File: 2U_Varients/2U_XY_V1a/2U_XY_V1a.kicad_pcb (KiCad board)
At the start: 4 copper layers, 83 x 212.6 mm, 32 parts, among them CN1 DF11-2DSA-4DP, J2 Conn_01x01, J3 Conn_01x01, J4 Conn_01x01, J5 Conn_01x01, U2 TMP112xxDRL, U3 DRV2605LDGS, U4 TCA4311ADGKR, U5 5040500691, U7 VEML6031X00

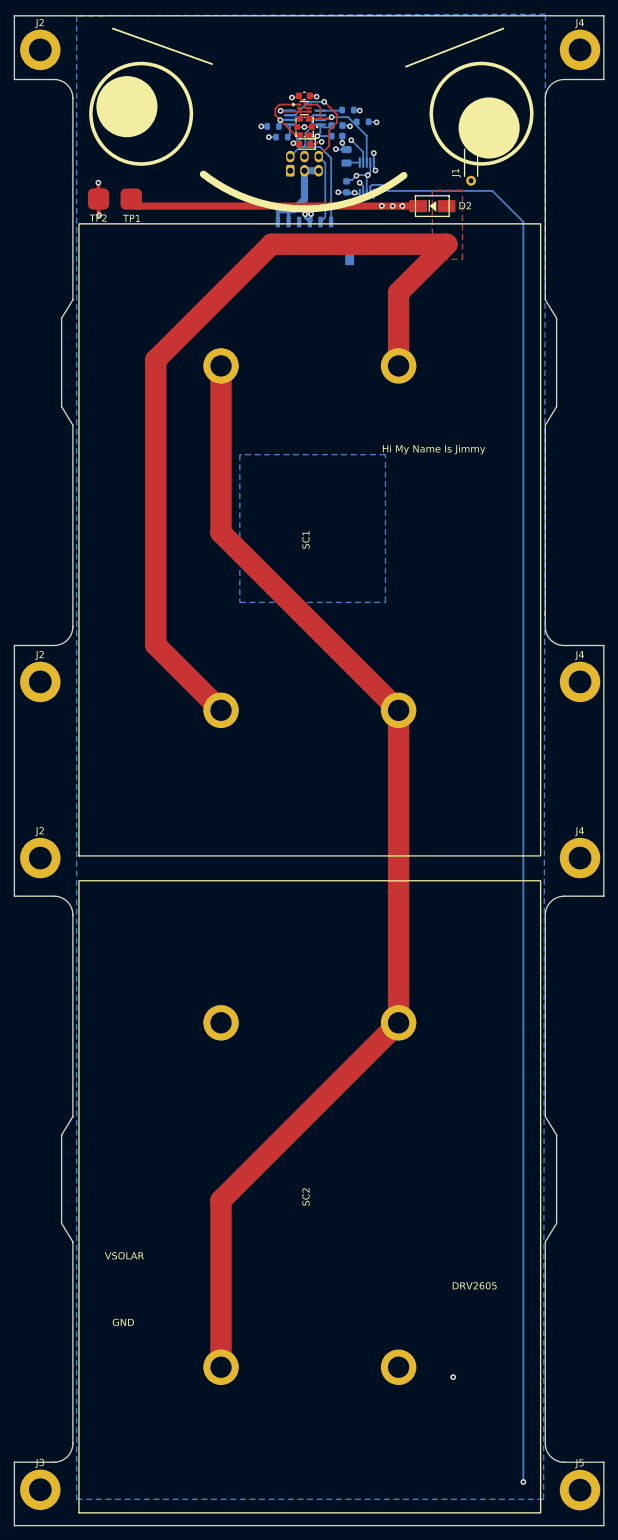
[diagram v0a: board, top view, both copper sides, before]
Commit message: Connector Adjustments
Moved away from the top of the Solar Face to the middle of the Solar Face
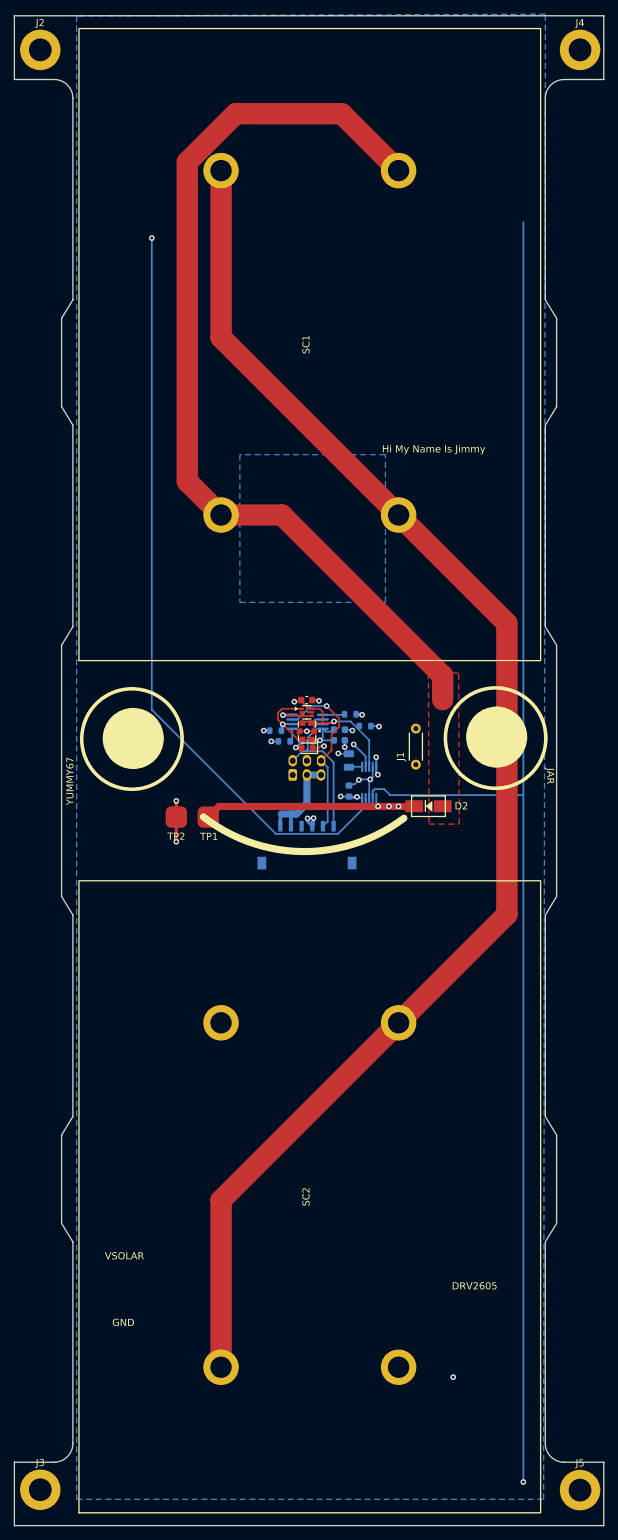
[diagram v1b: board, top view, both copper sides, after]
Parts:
- removed the J2 at (171.8, 154.8)
- removed the J2 at (171.8, 130.0)
- removed the J4 at (247.8, 154.8)
- removed the J4 at (247.8, 130.0)
- moved TP2 87.7 mm to (191.0, 149.0)
- moved TP1 87.7 mm to (195.5, 149.0)
- moved C2 85.1 mm to (209.3, 132.6)
- moved C3 85.1 mm to (215.3, 145.4)
- moved D4 85.1 mm to (209.4, 139.3)
- moved R2 85.1 mm to (206.2, 138.4)
- moved R4 85.1 mm to (215.5, 134.6)
- moved U3 85.1 mm to (218.1, 144.1)
- moved U4 85.1 mm to (209.4, 135.6)
- moved R6 85.1 mm to (217.5, 136.2)
- moved U2 85.1 mm to (209.3, 134.3)
- moved U5 85.1 mm to (209.3, 152.9)
- moved U7 85.1 mm to (209.3, 136.9)
- moved C4 85.1 mm to (213.9, 138.2)
- moved C5 85.1 mm to (215.3, 141.1)
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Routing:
- net Net-(U3-OUT+): track 20586.5 -> 20653.7 mm
- net Net-(SC1---Pad2): track 161.7 -> 201.8 mm
- net VSOLAR: track 55.9 -> 43.4 mm
- net /SOL_OUT: track 120.8 -> 131.5 mm
- net GND: track 26.8 -> 27.9 mm
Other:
- outline, holes or cut-outs redrawn
- board text added: "JAR"
- board text added: "V1a 2U Solar Panel Designed By: Michael Pham Reviewed By: William Hsu Modified By: Matthew Chang"
- board text added: "YUMMY67"
- board text removed: "V1a 2U Solar Panel Designed By: Michael Pham Reviewed By: William Hsu"

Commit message: Added GND and Clearance Holes
Moved clearance holes away and added 2 GND Vias for the Pico Molex Connector
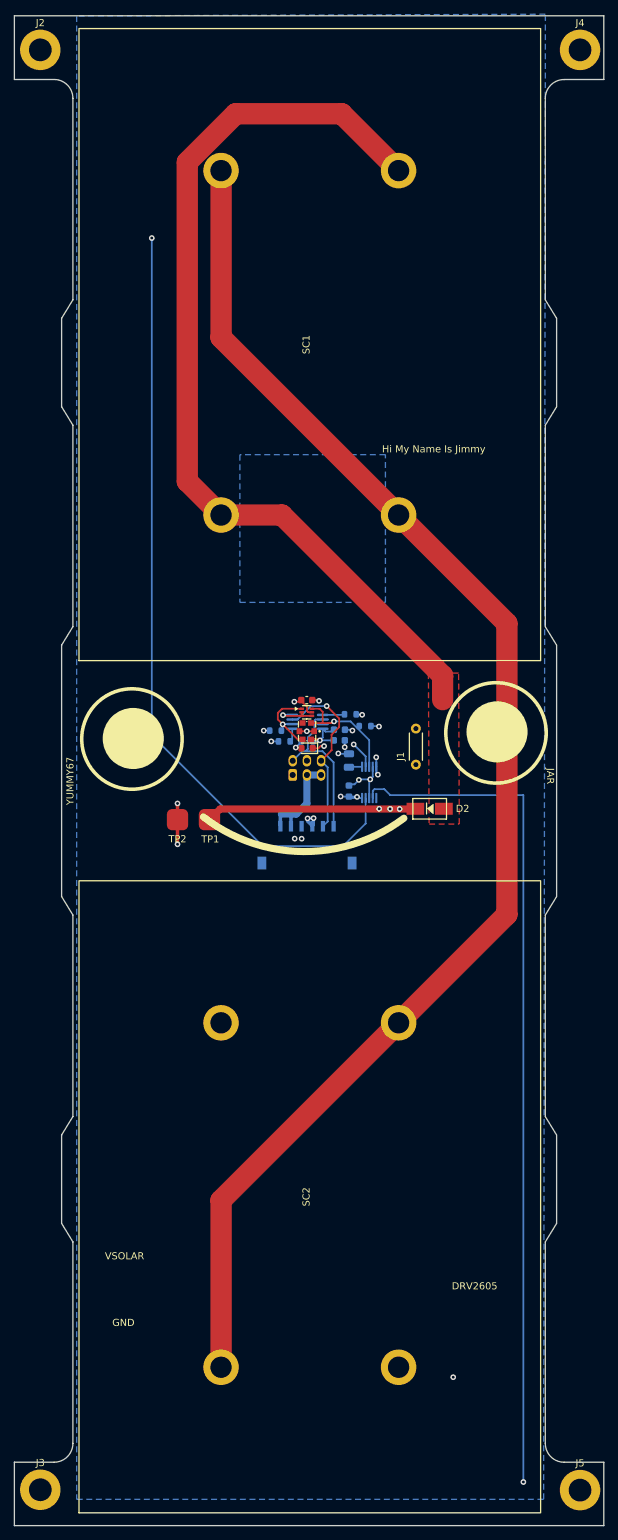
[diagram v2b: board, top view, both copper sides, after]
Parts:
- moved D2 0.40 mm to (226.6, 147.9)
- moved TP1 0.40 mm to (195.6, 149.4)
- moved TP2 0.40 mm to (191.1, 149.4)
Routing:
- net Net-(U3-OUT+): track 20653.7 -> 20577.9 mm
- net GND: vias 11 -> 13
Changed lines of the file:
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@@
 	(footprint "SolarPanelBoards:Test Pad"
 		(layer "F.Cu")
-		(at 195.455 149.03)
+		(at 195.620598 149.392774)
 		(property "Reference" "TP1"
 			(at 0.11 2.75 0)
@@
 	(footprint "SolarPanelBoards:Test Pad"
 		(layer "F.Cu")
-		(at 190.955 149.03)
+		(at 191.120598 149.392774)
 		(property "Reference" "TP2"
 			(at 0 2.730001 0)
@@
 	(footprint "SolarPanelBoards:DO-214AC"
 		(layer "F.Cu")
-		(at 226.454999 147.5)
+		(at 226.620597 147.862774)
 		(descr "Diode Footprint for CDBA240LL-HF")
 		(property "Reference" "D2"
@@
 	)
 	(gr_circle
-		(center 236.059037 137.767932)
-		(end 239.059037 140.767932)
+		(center 236.112301 137.03092)
+		(end 239.112301 140.03092)
 		(stroke
 			(width 0.12)
@@
 	)
 	(gr_circle
-		(center 235.914383 137.909693)
-		(end 240.914383 142.909693)
+		(center 235.967647 137.172681)
+		(end 240.967647 142.172681)
 		(stroke
 			(width 0.5)
@@
 	)
 	(segment
-		(start 190.955 146.75)
-		(end 190.955 149.03)
+		(start 191.120598 147.112774)
+		(end 191.120598 149.392774)
 		(width 0.5)
 		(layer "F.Cu")
@@
 	)
 	(segment
-		(start 190.955 152.5)
-		(end 190.955 149.03)
+		(start 191.120598 152.862774)
+		(end 191.120598 149.392774)
 		(width 0.5)
 		(layer "F.Cu")
@@
 	)
 	(via
+		(at 208.598908 152.076567)
+		(size 0.8)
+		(drill 0.4)
+		(layers "F.Cu" "B.Cu")
+		(free yes)
+		(net 1)
+	)
+	(via
 		(at 215.751297 136.846077)
 		(size 0.8)
@@
 	)
 	(via
-		(at 190.955 146.75)
+		(at 191.120598 147.112774)
 		(size 0.8)
 		(drill 0.4)
@@
 	)
 	(via
-		(at 190.955 152.5)
+		(at 191.120598 152.862774)
 		(size 0.8)
 		(drill 0.4)
@@
 	)
 	(via
+		(at 207.62098 152.066485)
+		(size 0.8)
+		(drill 0.4)
+		(layers "F.Cu" "B.Cu")
+		(free yes)
+		(net 1)
+	)
+	(via
 		(at 218.26 143.719999)
 		(size 0.8)
@@
 	)
 	(segment
-		(start 196.955 147.53)
-		(end 195.455 149.03)
+		(start 197.120598 147.892774)
+		(end 195.620598 149.392774)
 		(width 1)
 		(layer "F.Cu")
@@
 	)
 	(segment
-		(start 224.454998 147.53)
-		(end 196.955 147.53)
+		(start 224.620596 147.892774)
+		(end 197.120598 147.892774)
 		(width 1)
 		(layer "F.Cu")
@@
 	)
 	(via
-		(at 220.884998 147.52)
+		(at 221.050596 147.882774)
 		(size 0.8)
 		(drill 0.4)
@@
 	)
 	(via
-		(at 219.354998 147.5)
+		(at 219.520596 147.862774)
 		(size 0.8)
 		(drill 0.4)
@@
 	)
 	(via
-		(at 222.234998 147.53)
+		(at 222.400596 147.892774)
 		(size 0.8)
 		(drill 0.4)
@@
 	(segment
 		(start 217.610001 146.349999)
-		(end 217.610001 147.488002)
+		(end 217.610001 149.939001)
 		(width 0.25)
 		(layer "B.Cu")
@@
 	)
 	(segment
-		(start 239.82 145.939999)
-		(end 221.08 145.939999)
+		(start 217.610001 149.939001)
+		(end 214.42322 153.125782)
 		(width 0.25)
 		(layer "B.Cu")
@@
 	)
 	(segment
-		(start 220.24 145.099999)
-		(end 218.849998 145.099999)
+		(start 187.5 137.5)
+		(end 187.5 67.5)
 		(width 0.25)
 		(layer "B.Cu")
@@
 	)
 	(segment
-		(start 239.82 242.66)
-		(end 239.82 65.23)
+		(start 239.82 145.939999)
+		(end 221.08 145.939999)
 		(width 0.25)
 		(layer "B.Cu")
@@
 	)
 	(segment
-		(start 217.610001 147.488002)
-		(end 213.702004 151.395999)
+		(start 220.24 145.099999)
+		(end 218.849998 145.099999)
 		(width 0.25)
 		(layer "B.Cu")
@@
 	)
 	(segment
-		(start 218.849998 145.099999)
-		(end 218.609998 145.339999)
+		(start 203.125782 153.125782)
+		(end 187.5 137.5)
 		(width 0.25)
 		(layer "B.Cu")
@@
 	)
 	(segment
-		(start 187.5 133.921999)
-		(end 187.5 67.5)
+		(start 218.849998 145.099999)
+		(end 218.609998 145.339999)
 		(width 0.25)
 		(layer "B.Cu")
@@
 	)
 	(segment
-		(start 213.702004 151.395999)
-		(end 204.974 151.395999)
+		(start 239.82 145.939999)
+		(end 239.82 242.66)
 		(width 0.25)
 		(layer "B.Cu")
@@
 	)
 	(segment
-		(start 204.974 151.395999)
-		(end 187.5 133.921999)
+		(start 214.42322 153.125782)
+		(end 203.125782 153.125782)
 		(width 0.25)
 		(layer "B.Cu")
